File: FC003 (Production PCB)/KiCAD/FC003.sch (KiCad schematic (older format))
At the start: 58 parts, among them IC1 MSP430G2202, IC10 SC52-11, IC11 SC52-11, IC12 SC52-11, IC2 4017, IC3 74HC4060, IC4 ULN2803A, IC5 SC52-11, IC6 SC52-11, IC7 SC52-11, IC8 SC52-11, IC9 SC52-11, J1 JTAG, J2 IN, J3 PWR, J4 ACCESSORY, J5 EXT CLK, J6 HF SRC, SW1 DIPSW-8, X1 4.194304MHz

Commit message: Hardware Design finished Casing (SOB) added design/caes panelize added
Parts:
- added C8: 100uF/16V, C1P_D2.7, symbol CP
- added C9: 22uF/16V, C1P_D2.7, symbol CP
- added J15: PSU, PWR_3.5, symbol CONN_3
- added J16: EN_PR, HDR-2, symbol CONN_2
- added J17: IN_DIG, HDR-2, symbol CONN_2
- added U13: TS2950CT, TO-92_V, symbol TS2950CT
- J1: value JTAG -> SBW; symbol CONN_3 -> TI_SBW
- renumbered IC1 to U1, IC10 to U10, IC11 to U11, IC12 to U12, IC2 to U2, IC3 to U3, IC4 to U4, IC5 to U5, IC6 to U6, IC7 to U7, IC8 to U8, IC9 to U9
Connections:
- net GND: now also C8.2, C9.2, J15.1 (P1), J17.2 (PM), U13.2 (GND)
- net VCC: now also J1.4 (VCC), C9.1, U13.1 (VO)
- net at D10.2 (K), D9.1 (A), R5.2: now also J16.1 (P1); no longer U1.2 (P1.0), U1.6 (P1.4)
- net VDD: now reaches J4.12 (P12)
- net VDD: now also C8.1, J15.3 (P3), U13.3 (VI)
- new net: J16.2 (PM), J17.1 (P1), U1.2 (P1.0), U1.6 (P1.4)
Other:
- moved on the sheet: C5, R3

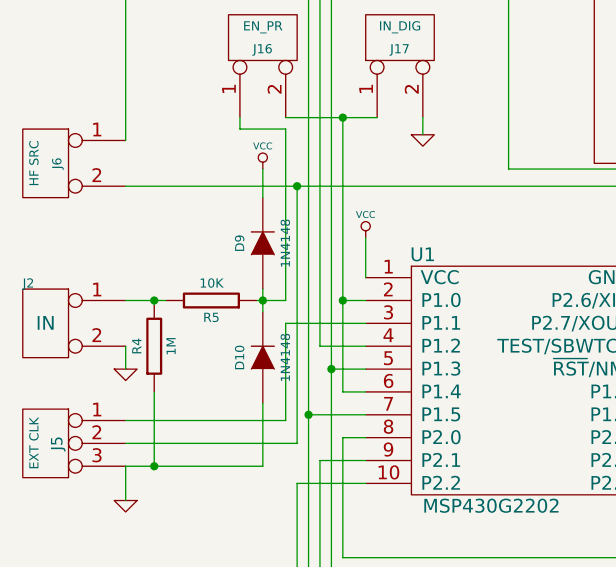
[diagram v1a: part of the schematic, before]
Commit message: Cost calculation added
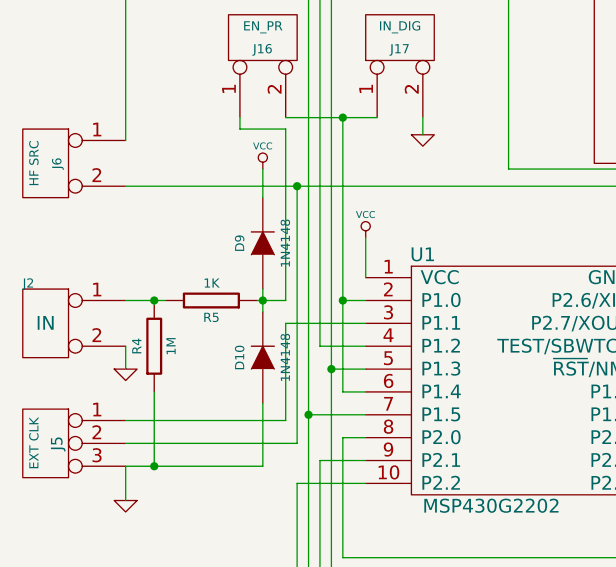
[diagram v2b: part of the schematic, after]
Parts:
- R5: value 10K -> 1K
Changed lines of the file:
@@
 Sheet 1 1
 Title "FC002B - Frequency Counter"
-Date "14 jan 2014"
+Date "31 jan 2014"
 Rev "1"
 Comp ""
@@
 P 1625 4425
 F 0 "R5" H 1625 4350 40  0000 C CNN
-F 1 "10K" H 1625 4500 40  0000 C CNN
+F 1 "1K" H 1625 4500 40  0000 C CNN
 F 2 "R2" H 1625 4425 60  0001 C CNN
 F 3 "~" H 1625 4425 60  0000 C CNN

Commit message: Add doc v0.3
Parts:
- C1, C2, C3, C4, C5, C6, C7: symbol C -> suf:C
- C8, C9: symbol CP -> suf:CP
- D1, D10, D2, D3, D4, D5, D6, D7, D8, D9: symbol DIODE -> device:DIODE
- J1: symbol TI_SBW -> suf:TI_SBW
- J10, J11, J12, J13, J14, J7, J8, J9: symbol JUMPER -> suf:JUMPER
- J15, J5: symbol CONN_3 -> conn1:CONN_3
- J16, J17, J2, J3, J6: symbol CONN_2 -> conn1:CONN_2
- J4: symbol CONN_14 -> conn1:CONN_14
- R1, R12, R13, R14, R15, R16, R17, R18, R19, R2, R3, R4, R5: symbol R -> suf:R
- SW1: symbol DIPSW-8 -> suf:DIPSW-8
- U1: symbol MSP430G2553 -> suf:MSP430G2553
- U10, U11, U12, U5, U6, U7, U8, U9: symbol 7SEGMENT_CC -> suf:7SEGMENT_CC
- U13: symbol TS2950CT -> suf:TS2950CT
- U2: symbol 4017 -> suf:4017
- U3: symbol 74HC4060 -> suf:74HC4060
- U4: symbol ULN2803A -> suf:ULN2803A
- X1: symbol CRYSTAL -> device:CRYSTAL
